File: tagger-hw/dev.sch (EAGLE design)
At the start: 55 parts, among them J2 22-23-2021, J3 22-23-2021, X1 EXC-31B

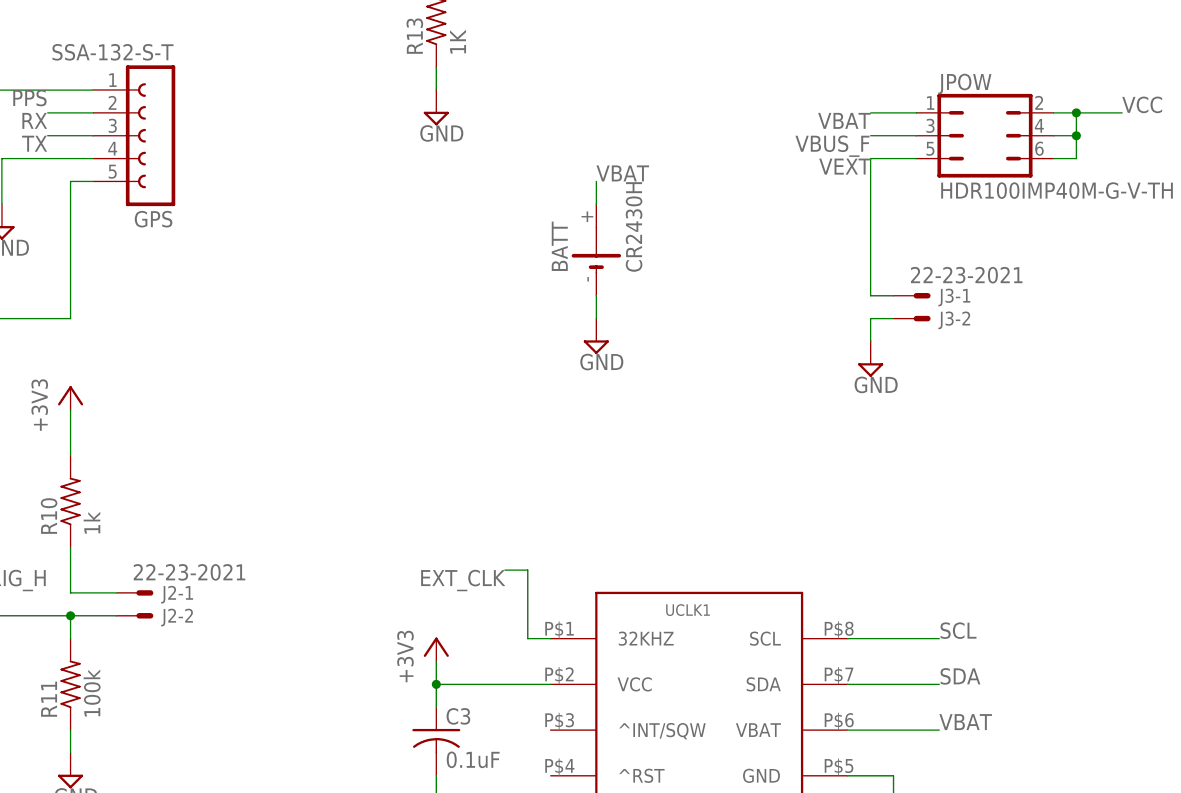
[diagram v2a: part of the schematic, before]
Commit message: Switch to CR2032
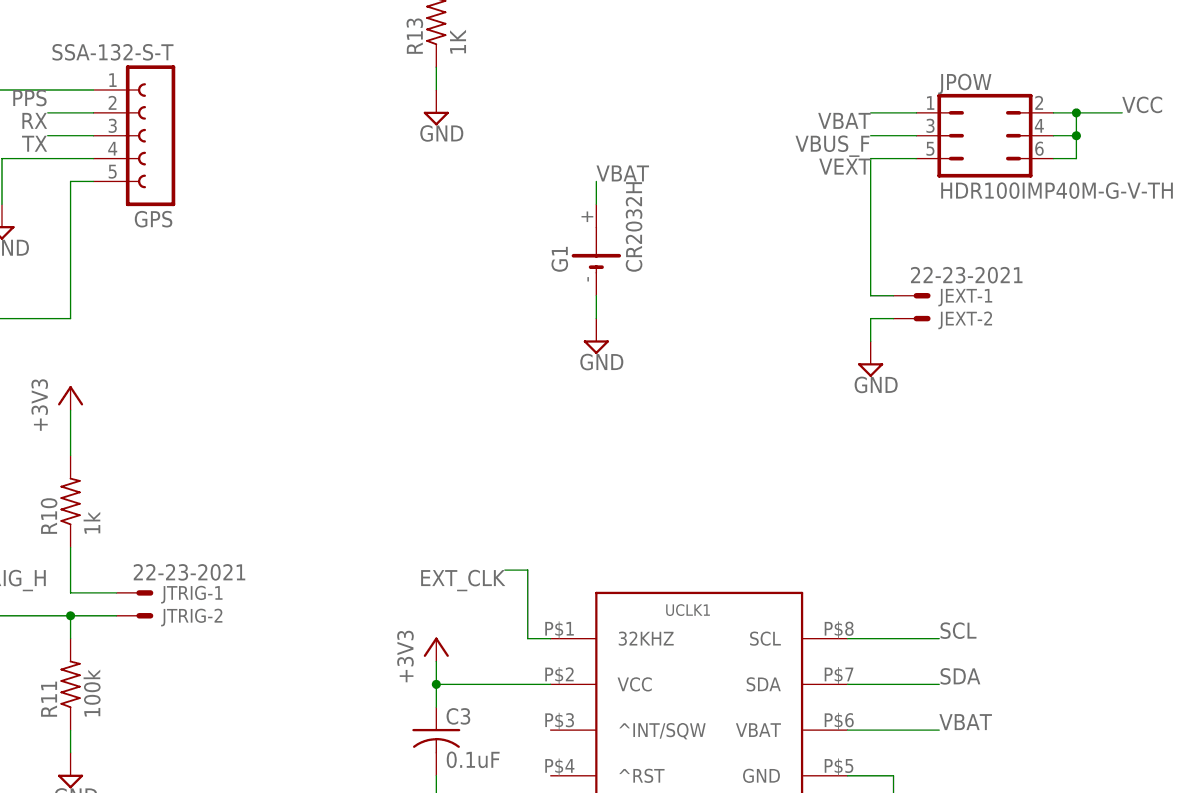
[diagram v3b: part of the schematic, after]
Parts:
- removed BATT: CR2430H, battery:CR2430H
- added G1: CR2032H, battery:CR2032H
- C2, C3, C9: device adafruit:C-USC0805K -> adafruit:C-USC0603K
- renumbered J2 to JTRIG, J3 to JEXT
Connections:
- net GND: now also G1.-; no longer BATT.-
- net VBAT: now also G1.+; no longer BATT.+

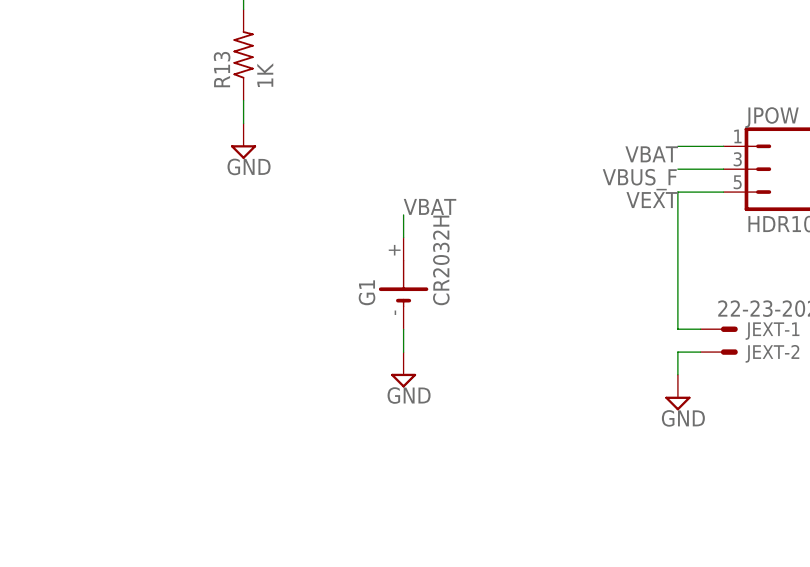
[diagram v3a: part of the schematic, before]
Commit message: Update to a non-esoteric battery holder
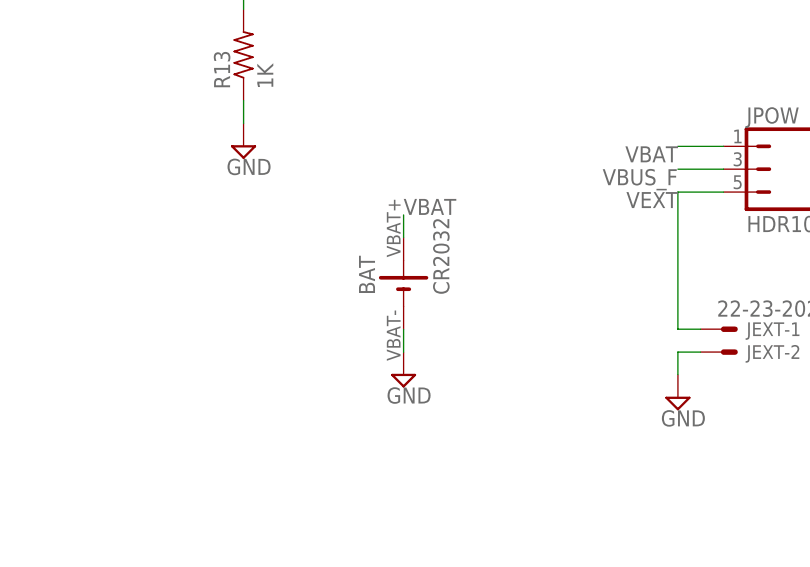
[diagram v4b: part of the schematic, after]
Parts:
- removed G1: CR2032H, battery:CR2032H
- added BAT: CR2032, dorskyee:CR2032
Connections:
- net GND: now also BAT.-; no longer G1.-
- net VBAT: now also BAT.+; no longer G1.+
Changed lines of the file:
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@@
 <part name="SDA" library="adafruit" deviceset="PINHD-1X1" device=""/>
 <part name="SCL" library="adafruit" deviceset="PINHD-1X1" device=""/>
-<part name="G1" library="battery" library_urn="urn:adsk.eagle:library:109" deviceset="CR2032H" device="" package3d_urn="urn:adsk.eagle:package:4585/1"/>
+<part name="BAT" library="dorskyee" deviceset="CR2032" device=""/>
 </parts>
 <sheets>
@@
 <instance part="SDA" gate="G$1" x="12.7" y="-111.76"/>
 <instance part="SCL" gate="G$1" x="50.8" y="-111.76"/>
-<instance part="G1" gate="1" x="83.82" y="-12.7" rot="R90"/>
+<instance part="BAT" gate="G$1" x="83.82" y="-12.7" rot="R90"/>
 </instances>
 <busses>
@@
 <pinref part="SUPPLY16" gate="GND" pin="GND"/>
 <wire x1="83.82" y1="-20.32" x2="83.82" y2="-17.78" width="0.1524" layer="91"/>
-<pinref part="G1" gate="1" pin="-"/>
+<pinref part="BAT" gate="G$1" pin="-"/>
 </segment>
 <segment>
@@
 <wire x1="83.82" y1="-7.62" x2="83.82" y2="-5.08" width="0.1524" layer="91"/>
 <label x="83.82" y="-5.08" size="1.778" layer="95"/>
-<pinref part="G1" gate="1" pin="+"/>
-</segment>
-</net>
+<pinref part="BAT" gate="G$1" pin="+"/>
+</segment>
+</net>
